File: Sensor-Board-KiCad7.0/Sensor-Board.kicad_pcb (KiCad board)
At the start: 2 copper layers, 75.4 x 75.4 mm, 128 parts, among them J2 B04B-XASK-1, U1 OPA396DCKT, U10 BME680, U11 OPA396DCKT, U12 OPA396DCKT, U14 OPA396DCKT, U15 MMBFJ177LT1, U16 MMBFJ177LT1, U17 MMBFJ177LT1, U18 NAU7802SGI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

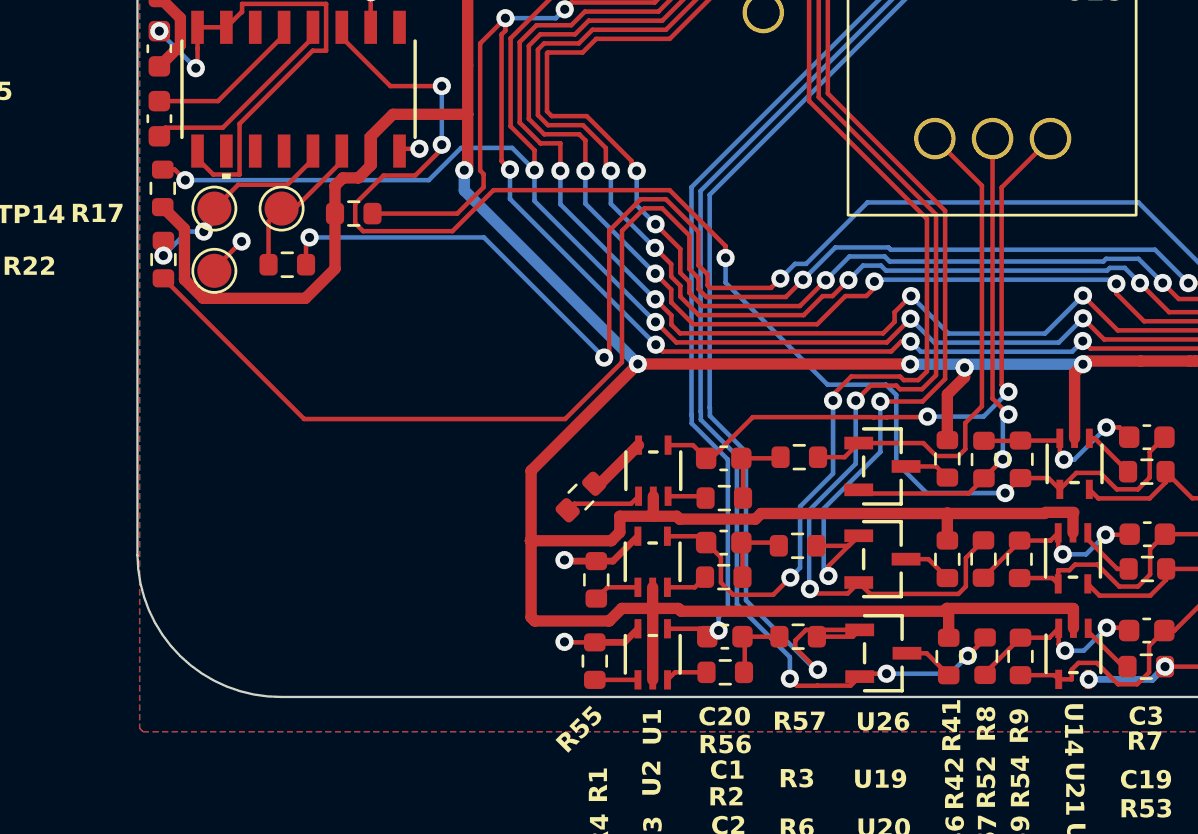
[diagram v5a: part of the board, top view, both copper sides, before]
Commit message: Updated gas collection cell drawing
Updated GCC drawing to bring it to actual size
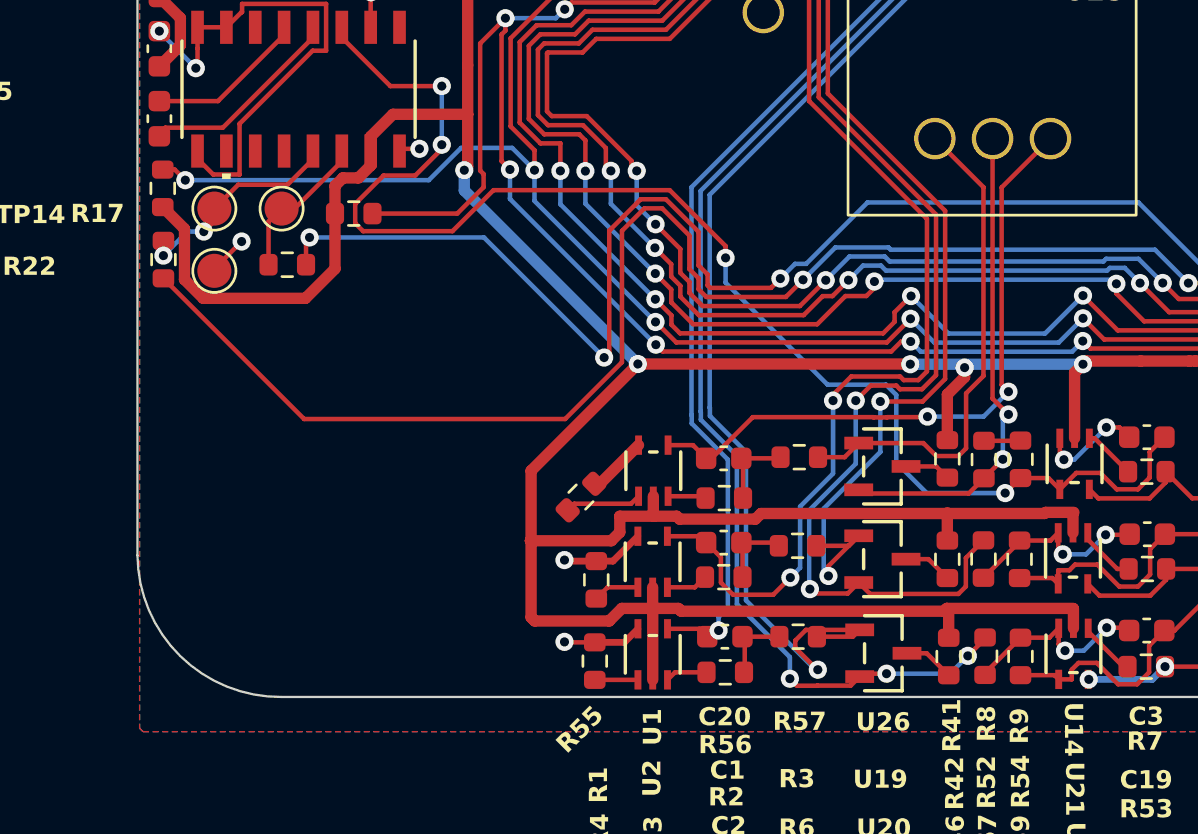
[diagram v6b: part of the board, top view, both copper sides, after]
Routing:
- net Net-(U14--IN): track 8.04 -> 6.27 mm

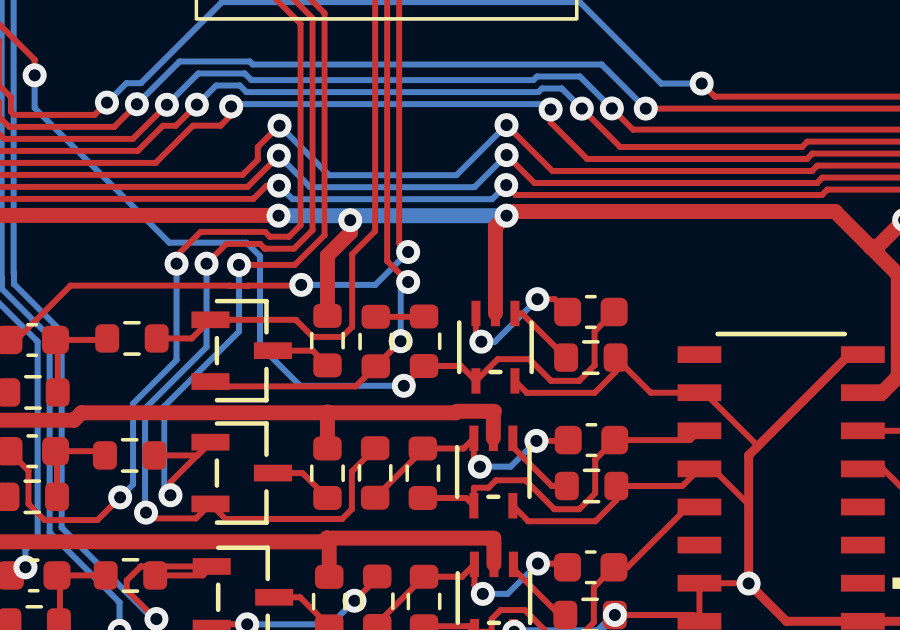
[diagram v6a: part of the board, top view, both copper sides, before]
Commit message: Fixed broken connection
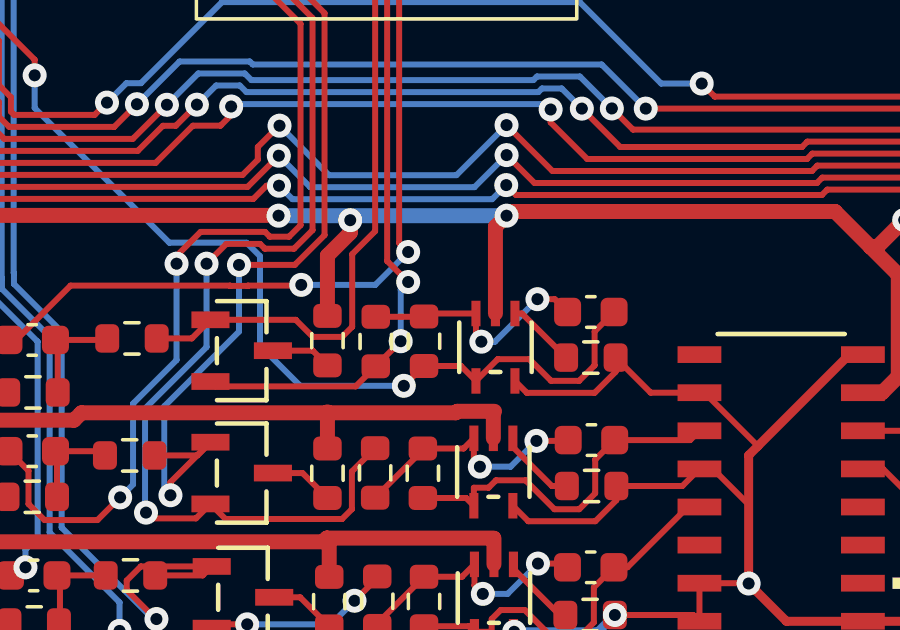
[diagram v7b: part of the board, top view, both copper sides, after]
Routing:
- net Net-(U14--IN): track 6.27 -> 8.04 mm
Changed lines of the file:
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@@
   (segment (start 113.35 106.44) (end 113.35 109.02) (width 0.2) (layer "B.Cu") (net 5))
   (segment (start 125.84 115.09) (end 130.33 119.58) (width 0.2) (layer "B.Cu") (net 5))
+  (segment (start 140.550013 121.94) (end 138.92 121.94) (width 0.2) (layer "F.Cu") (net 6))
   (segment (start 142.600107 121.462295) (end 143.177295 121.462295) (width 0.2) (layer "F.Cu") (net 6))
   (segment (start 140.550013 121.94) (end 140.550013 122.700013) (width 0.2) (layer "F.Cu") (net 6))
+  (segment (start 138.92 121.94) (end 138.82 122.04) (width 0.2) (layer "F.Cu") (net 6))
   (segment (start 137.21 122.05) (end 138.81 122.05) (width 0.2) (layer "F.Cu") (net 6))
   (segment (start 138.81 122.05) (end 138.82 122.04) (width 0.2) (layer "F.Cu") (net 6))
@@
       a4a177f7-c4e3-4962-a8e1-1ba69e731e3c
       a715a153-91fb-4c12-990d-8f2d29e75816
-      a7f20b61-cecc-4ccb-b843-9687bdac4e62
       a8a950a6-6f13-4a84-a168-0ab154c006df
       aa3763b2-5b1d-4a63-bac3-b709fa6f48a3
@@
       c8057777-eb6b-4028-9d59-431979389eea
       caef189a-5280-485a-b3fa-c3ecbce05574
-      ccf50011-bfd5-4e73-85d5-c06186823ffb
       ce087d24-31a8-4e16-a275-0c9ea34a3d96
       ce52c662-fb76-40d3-9358-8ba3bf144519
@@
       e49d32fc-4f5f-4efe-8c66-456dfc03708c
       e7586561-0a6c-419d-8198-4e3654c9f0b2
-      e77c9616-f955-4714-9eea-4766f00f2ada
       e7cee15e-6751-4ec9-add0-419ff576bd72
       e8b3b68c-099b-4916-9cfd-6bf7f5980119

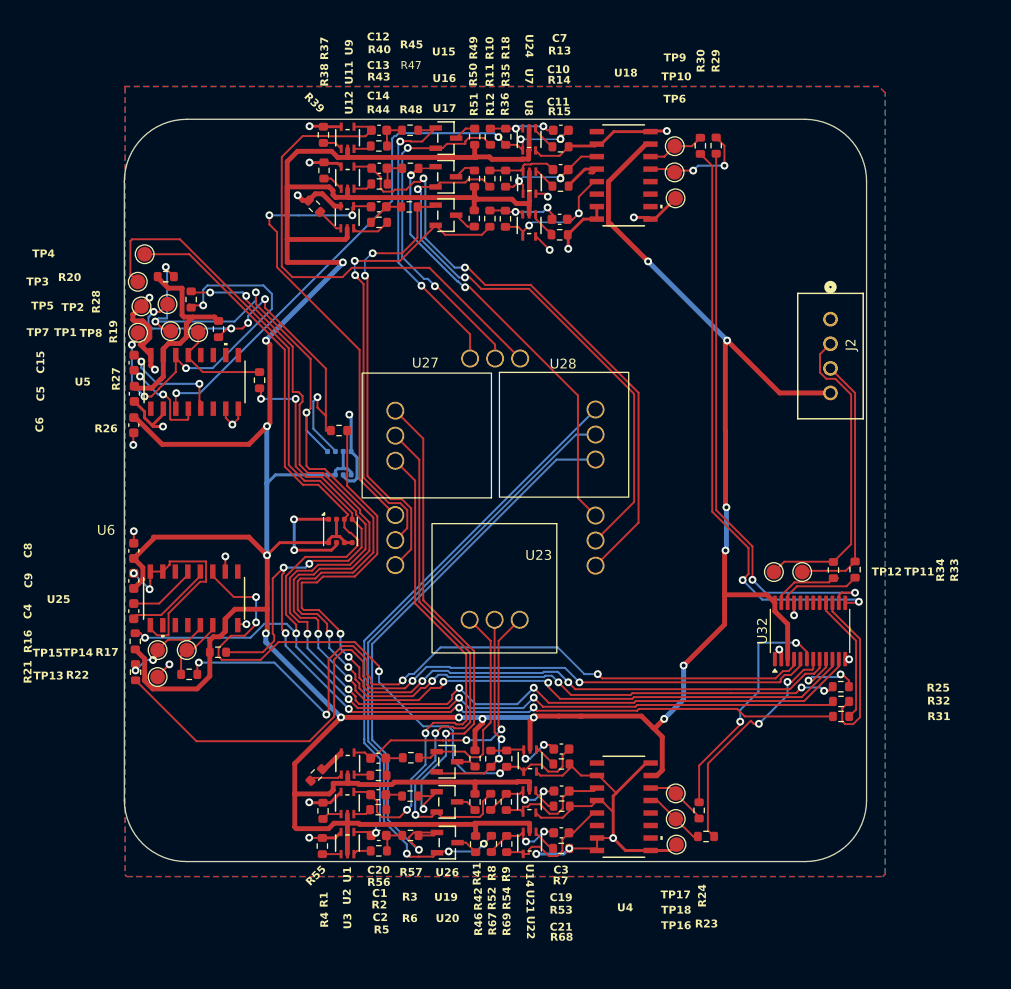
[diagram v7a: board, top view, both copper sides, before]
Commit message: Updating component positioning for 1mm clearance around gas collection cell
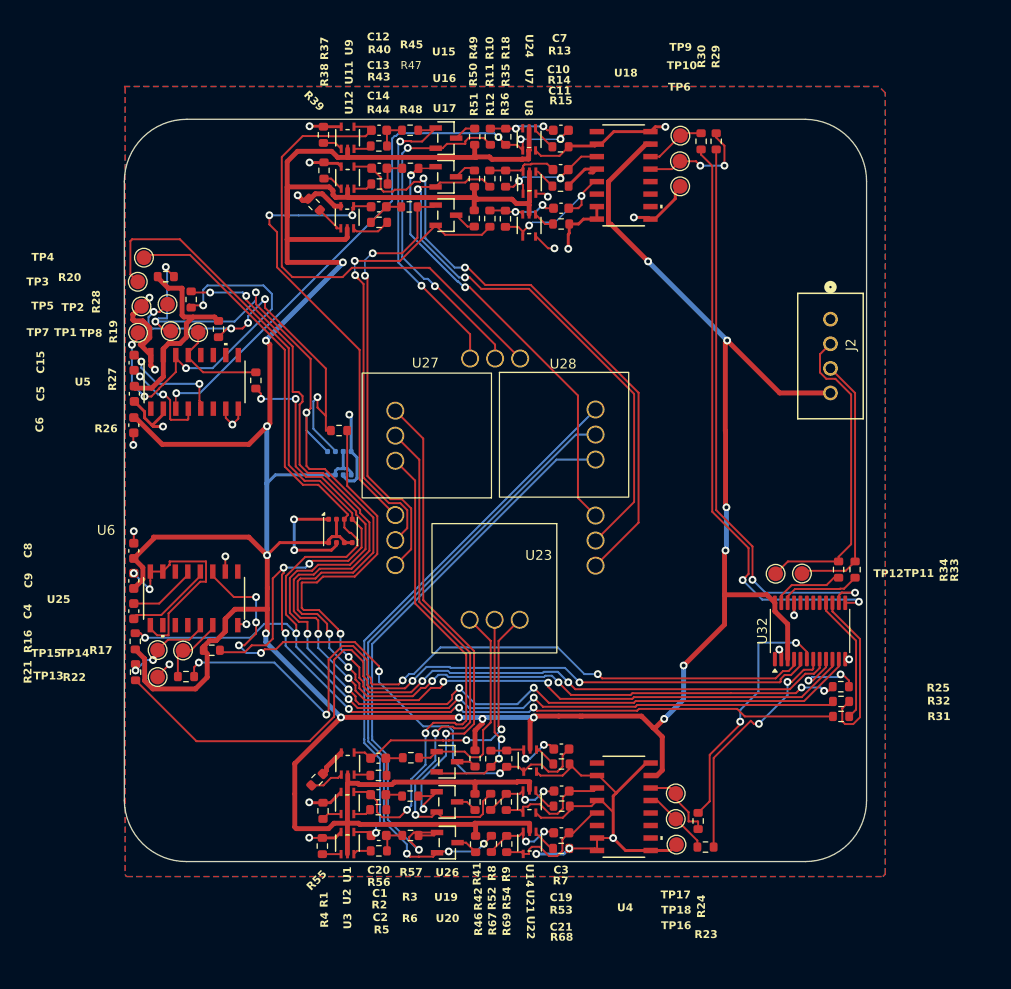
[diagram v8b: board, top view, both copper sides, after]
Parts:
- moved TP6 1.31 mm to (156.4, 64.7)
- moved TP10 1.25 mm to (156.4, 62.1)
- moved TP9 1.21 mm to (156.5, 59.5)
- moved C11 1.13 mm to (144.3, 66.9)
- moved R15 1.11 mm to (144.3, 68.5)
- moved R24 1.08 mm to (158.3, 129.2)
- moved R23 1.08 mm to (159.0, 131.8)
- moved R17 0.66 mm to (108.8, 111.8)
- moved R34 0.53 mm to (172.6, 103.7)
- moved R55 0.48 mm to (119.5, 125.0)
- moved R30 0.46 mm to (158.6, 60.1)
- moved R29 0.44 mm to (160.1, 60.1)
- moved R22 0.40 mm to (106.2, 114.5)
- moved TP14 0.38 mm to (105.9, 111.9)
- moved R27 0.38 mm to (113.3, 84.4)
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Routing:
- net AOut1_NO2: track 61.4 -> 56.7 mm, vias 4 -> 6
- net +3.3V: track 455.5 -> 452.5 mm
- net GND: track 177.6 -> 180.2 mm
- net ADC1_SDA: track 6.67 -> 8.42 mm
- net ADC2_SDA: track 6.31 -> 7.90 mm
- net Net-(U32-SD1): track 24.7 -> 25.8 mm
- net ADC2_SCL: track 6.32 -> 7.09 mm
- net MUX_SCL: track 26.5 -> 27.2 mm
- net Net-(U32-SD0): track 76.8 -> 77.4 mm
- net Net-(U32-SC1): track 24.4 -> 25.0 mm
